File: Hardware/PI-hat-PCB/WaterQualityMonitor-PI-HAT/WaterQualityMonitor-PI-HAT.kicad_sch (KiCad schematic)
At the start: 29 parts

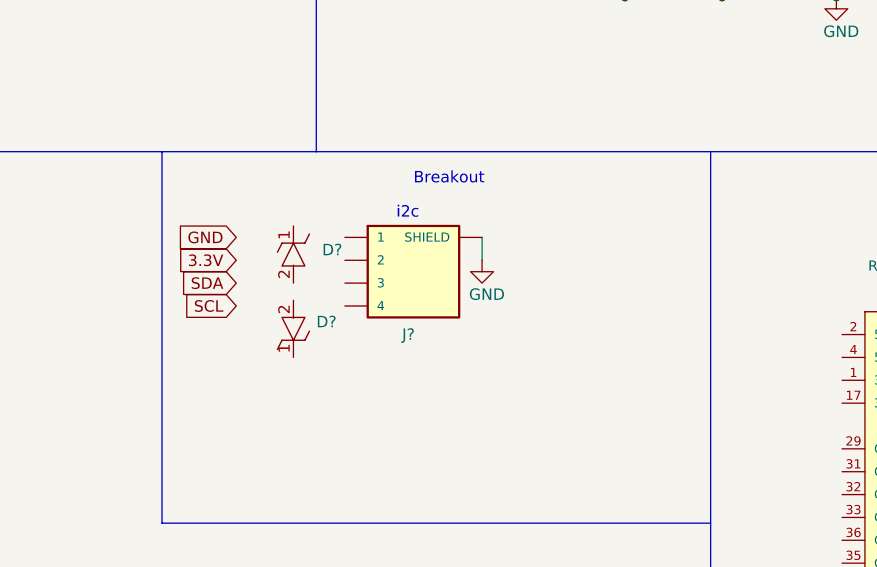
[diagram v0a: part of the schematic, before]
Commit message: updated i2c esd protection circuit
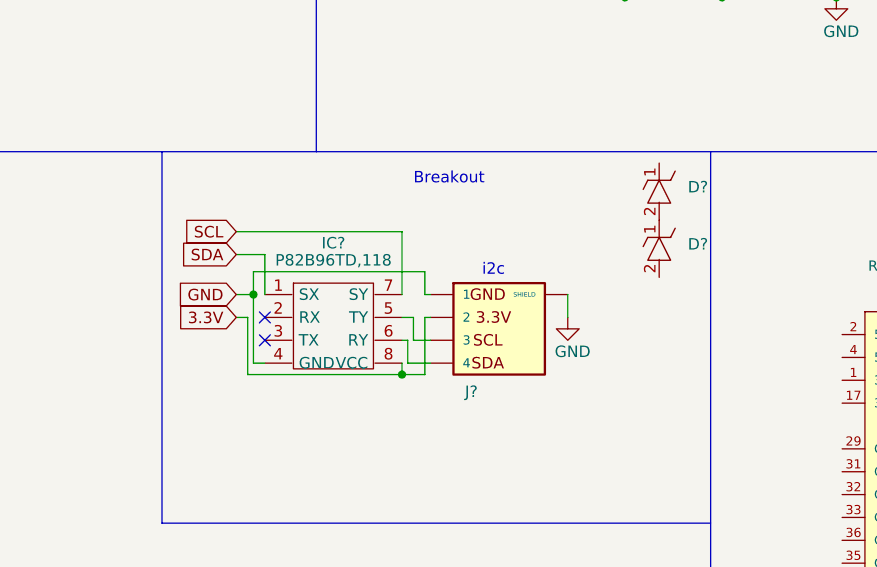
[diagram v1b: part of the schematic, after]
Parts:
- added IC?: P82B96TD,118, SOIC127P600X175-8N, symbol SamacSys_Parts:P82B96TD,118
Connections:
- net 3.3V: now also J?.2, IC?.8 (VCC)
- net GND: now also J?.1, IC?.4 (GND)
- net SCL: now also IC?.7 (SY)
- net SDA: now also IC?.1 (SX)
- net at D?.2: now also D?.1
- net at J?.3: now also IC?.5 (TY)
- net at J?.4: now also IC?.6 (RY)
- no-connect marks 0 -> 2
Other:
- moved on the sheet: D?

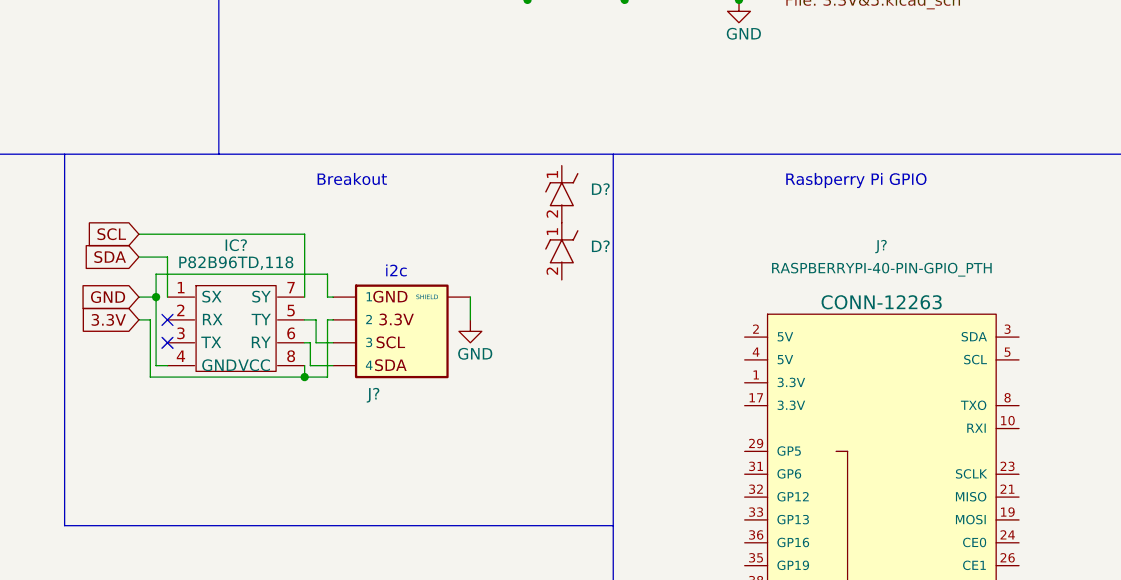
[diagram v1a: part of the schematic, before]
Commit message: fixed i2c circuit
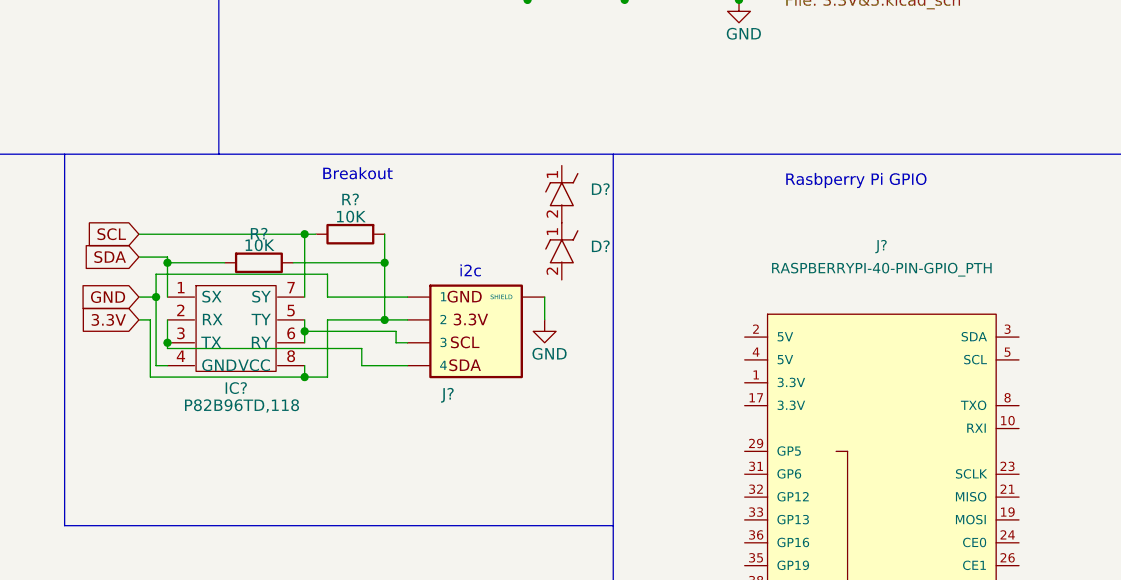
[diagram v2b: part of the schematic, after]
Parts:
- added R? (x2): 10K, symbol Device:R
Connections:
- net 3.3V: now also R?.1, R?.2
- net SCL: now also R?.1
- net SDA: now also R?.2
- net at IC?.2 (RX): now also IC?.3 (TX), J?.4
- net at IC?.5 (TY), J?.3: now also IC?.6 (RY)
- no-connect marks 2 -> 0
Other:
- moved on the sheet: J?

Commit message: log updated
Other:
- note added: "I2C Breakout"
- note removed: "Breakout"
- moved on the sheet: F?
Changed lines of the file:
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@@
     (stroke (width 0) (type default) (color 0 0 0 0))
   )
-  (wire (pts (xy 205.105 32.385) (xy 208.915 32.385))
+  (wire (pts (xy 205.105 32.385) (xy 206.248 32.385))
     (stroke (width 0) (type default) (color 0 0 0 0))
   )
@@
     (stroke (width 0) (type default) (color 0 0 0 0))
   )
+  (wire (pts (xy 213.868 32.385) (xy 216.535 32.385))
+    (stroke (width 0) (type default) (color 0 0 0 0))
+  )
   (wire (pts (xy 63.5 71.755) (xy 67.945 71.755))
     (stroke (width 0) (type default) (color 0 0 0 0))
@@
     (stroke (width 0) (type default) (color 0 0 0 0))
   )
-  (text "Breakout\n" (at 193.675 75.565 0)
+  (text "I2C Breakout\n" (at 187.96 75.565 0)
     (effects (font (size 1.27 1.27)) (justify left bottom))
   )
@@
     (pin "2")
   )
-  (symbol (lib_id "Device:Fuse") (at 212.725 32.385 90) (unit 1)
-    (in_bom yes) (on_board yes) (fields_autoplaced)
-    (property "Reference" "F?" (id 0) (at 212.725 26.035 90))
-    (property "Value" "10A" (id 1) (at 212.725 28.575 90))
-    (property "Footprint" "" (id 2) (at 212.725 34.163 90)
-      (effects (font (size 1.27 1.27)) hide)
-    )
-    (property "Datasheet" "~" (id 3) (at 212.725 32.385 0)
-      (effects (font (size 1.27 1.27)) hide)
-    )
+  (symbol (lib_id "Device:Fuse") (at 210.058 32.385 90) (unit 1)
+    (in_bom yes) (on_board yes) (fields_autoplaced)
+    (property "Reference" "F?" (id 0) (at 210.058 26.035 90))
+    (property "Value" "10A" (id 1) (at 210.058 28.575 90))
+    (property "Footprint" "" (id 2) (at 210.058 34.163 90)
+      (effects (font (size 1.27 1.27)) hide)
+    )
+    (property "Datasheet" "~" (id 3) (at 210.058 32.385 0)
+      (effects (font (size 1.27 1.27)) hide)
+    )

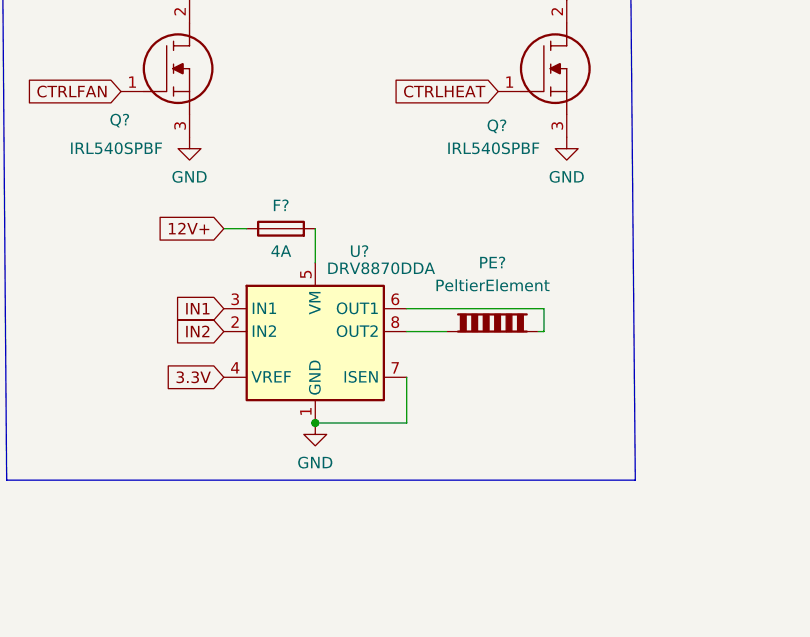
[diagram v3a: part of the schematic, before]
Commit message: Updated H-bridge schematic + Use case diagram
 included decoupling capacitors
Started working on use case diagram
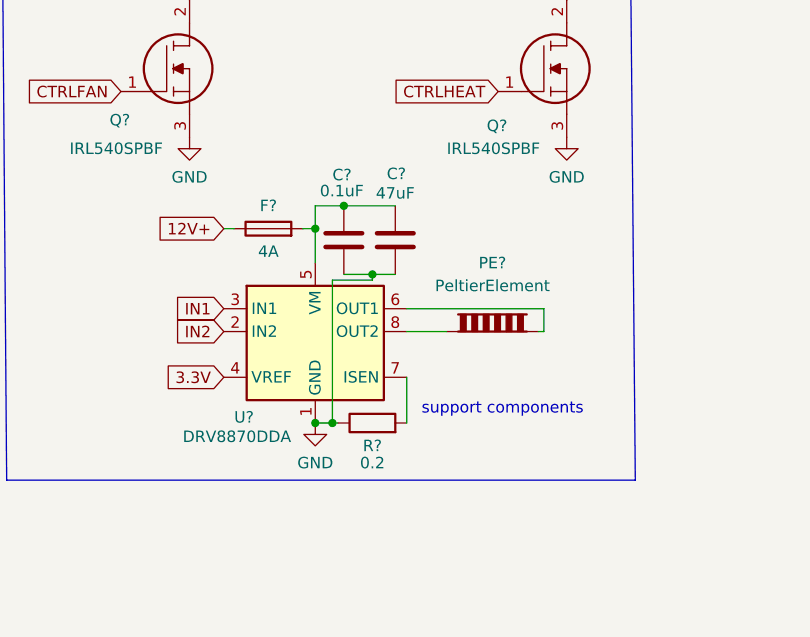
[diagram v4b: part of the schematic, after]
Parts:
- added C?: 47uF, symbol Device:C
- added C?: 0.1uF, symbol Device:C
- added R?: 0.2, symbol Device:R
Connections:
- net GND: now also C?.1, C?.1, R?.1; no longer U?.7 (ISEN)
- net at F?.2, U?.5 (VM): now also C?.2, C?.2
- new net: R?.2, U?.7 (ISEN)
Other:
- note added: "support components"
- moved on the sheet: F?
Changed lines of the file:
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@@
   (junction (at 56.515 27.305) (diameter 0) (color 0 0 0 0)
   )
+  (junction (at 47.625 114.3) (diameter 0) (color 0 0 0 0)
+  )
   (junction (at 30.48 27.305) (diameter 0) (color 0 0 0 0)
   )
@@
   (junction (at 176.53 93.345) (diameter 0) (color 0 0 0 0)
   )
+  (junction (at 53.975 119.38) (diameter 0) (color 0 0 0 0)
+  )
   (junction (at 227.33 55.245) (diameter 0) (color 0 0 0 0)
   )
+  (junction (at 49.53 135.89) (diameter 0) (color 0 0 0 0)
+  )
   (junction (at 175.26 88.265) (diameter 0) (color 0 0 0 0)
   )
+  (junction (at 50.8 111.76) (diameter 0) (color 0 0 0 0)
+  )
   (junction (at 67.818 27.305) (diameter 0) (color 0 0 0 0)
   )
@@
     (stroke (width 0) (type default) (color 0 0 0 0))
   )
+  (wire (pts (xy 53.975 120.015) (xy 49.53 120.015))
+    (stroke (width 0) (type default) (color 0 0 0 0))
+  )
   (polyline (pts (xy 82.55 72.39) (xy 182.245 72.39))
     (stroke (width 0) (type default) (color 0 0 0 0))
@@
     (stroke (width 0) (type default) (color 0 0 0 0))
   )
+  (wire (pts (xy 49.53 135.89) (xy 50.165 135.89))
+    (stroke (width 0) (type default) (color 0 0 0 0))
+  )
   (wire (pts (xy 60.96 45.72) (xy 75.184 45.72))
     (stroke (width 0) (type default) (color 0 0 0 0))
@@
     (stroke (width 0) (type default) (color 0 0 0 0))
   )
-  (wire (pts (xy 37.465 114.3) (xy 40.005 114.3))
+  (wire (pts (xy 47.625 135.89) (xy 49.53 135.89))
+    (stroke (width 0) (type default) (color 0 0 0 0))
+  )
+  (wire (pts (xy 37.465 114.3) (xy 38.608 114.3))
     (stroke (width 0) (type default) (color 0 0 0 0))
   )
@@
     (stroke (width 0) (type default) (color 0 0 0 0))
   )
+  (wire (pts (xy 49.53 120.015) (xy 49.53 135.89))
+    (stroke (width 0) (type default) (color 0 0 0 0))
+  )
   (wire (pts (xy 216.535 55.245) (xy 227.33 55.245))
     (stroke (width 0) (type default) (color 0 0 0 0))
@@
     (stroke (width 0) (type default) (color 0 0 0 0))
   )
+  (wire (pts (xy 53.975 119.38) (xy 56.515 119.38))
+    (stroke (width 0) (type default) (color 0 0 0 0))
+  )
   (wire (pts (xy 174.625 97.155) (xy 191.77 97.155))
     (stroke (width 0) (type default) (color 0 0 0 0))
@@
     (stroke (width 0) (type default) (color 0 0 0 0))
   )
+  (wire (pts (xy 47.625 114.3) (xy 47.625 111.76))
+    (stroke (width 0) (type default) (color 0 0 0 0))
+  )
   (wire (pts (xy 173.355 88.265) (xy 175.26 88.265))
     (stroke (width 0) (type default) (color 0 0 0 0))
@@
     (stroke (width 0) (type default) (color 0 0 0 0))
   )
+  (wire (pts (xy 50.8 111.76) (xy 56.515 111.76))
+    (stroke (width 0) (type default) (color 0 0 0 0))
+  )
   (wire (pts (xy 57.785 130.81) (xy 57.785 135.89))
     (stroke (width 0) (type default) (color 0 0 0 0))
@@
     (stroke (width 0) (type default) (color 0 0 0 0))
   )
+  (wire (pts (xy 53.975 119.38) (xy 53.975 120.015))
+    (stroke (width 0) (type default) (color 0 0 0 0))
+  )
   (wire (pts (xy 175.26 85.725) (xy 194.31 85.725))
     (stroke (width 0) (type default) (color 0 0 0 0))
   )
+  (wire (pts (xy 50.8 119.38) (xy 53.975 119.38))
+    (stroke (width 0) (type default) (color 0 0 0 0))
+  )
   (wire (pts (xy 19.05 27.305) (xy 22.86 27.305))
     (stroke (width 0) (type default) (color 0 0 0 0))
@@
     (stroke (width 0) (type default) (color 0 0 0 0))
   )
-  (wire (pts (xy 57.785 135.89) (xy 47.625 135.89))
-    (stroke (width 0) (type default) (color 0 0 0 0))
-  )
   (wire (pts (xy 56.515 27.305) (xy 56.515 38.1))
     (stroke (width 0) (type default) (color 0 0 0 0))
@@
     (stroke (width 0) (type default) (color 0 0 0 0))
   )
+  (wire (pts (xy 47.625 111.76) (xy 50.8 111.76))
+    (stroke (width 0) (type default) (color 0 0 0 0))
+  )
   (wire (pts (xy 191.77 90.805) (xy 191.77 92.075))
     (stroke (width 0) (type default) (color 0 0 0 0))
   )
   (polyline (pts (xy 226.06 72.39) (xy 226.06 164.465))
+    (stroke (width 0) (type default) (color 0 0 0 0))
+  )
+  (wire (pts (xy 46.228 114.3) (xy 47.625 114.3))
     (stroke (width 0) (type default) (color 0 0 0 0))
   )
@@
   )
   (text "Motors" (at 133.35 16.51 0)
+    (effects (font (size 1.27 1.27)) (justify left bottom))
+  )
+  (text "support components\n" (at 59.436 135.128 0)
     (effects (font (size 1.27 1.27)) (justify left bottom))
   )
@@
       (effects (font (size 1.27 1.27)) (justify right) hide)
     )
+  )
+  (symbol (lib_id "Device:C") (at 56.515 115.57 180) (unit 1)
+    (in_bom yes) (on_board yes)
+    (property "Reference" "C?" (id 0) (at 56.642 108.204 0))
+    (property "Value" "47uF" (id 1) (at 56.515 110.363 0))
+    (property "Footprint" "" (id 2) (at 55.5498 111.76 0)
+      (effects (font (size 1.27 1.27)) hide)
+    )
+    (property "Datasheet" "~" (id 3) (at 56.515 115.57 0)
+      (effects (font (size 1.27 1.27)) hide)
+    )
+    (pin "1")
+    (pin "2")
   )
   (symbol (lib_id "Connector:Screw_Terminal_01x04") (at 179.705 28.575 0) (unit 1)
@@
     (pin "7")
     (pin "8")
+  )
+  (symbol (lib_id "Device:C") (at 50.8 115.57 180) (unit 1)
+    (in_bom yes) (on_board yes)
+    (property "Reference" "C?" (id 0) (at 49.53 108.331 0)
+      (effects (font (size 1.27 1.27)) (justify right))
+    )
+    (property "Value" "0.1uF" (id 1) (at 48.133 110.109 0)
+      (effects (font (size 1.27 1.27)) (justify right))
+    )
+    (property "Footprint" "" (id 2) (at 49.8348 111.76 0)
+      (effects (font (size 1.27 1.27)) hide)
+    )
+    (property "Datasheet" "~" (id 3) (at 50.8 115.57 0)
+      (effects (font (size 1.27 1.27)) hide)
+    )
+    (pin "1")
+    (pin "2")
   )
   (symbol (lib_id "SparkFun-Connectors:RASPBERRYPI-40-PIN-GPIO_PTH") (at 255.905 120.65 0) (unit 1)
@@
     (pin "2")
   )
-  (symbol (lib_id "Device:Fuse") (at 43.815 114.3 90) (unit 1)
-    (in_bom yes) (on_board yes)
-    (property "Reference" "F?" (id 0) (at 43.815 111.76 90))
-    (property "Value" "4A" (id 1) (at 43.815 116.84 90))
-    (property "Footprint" "" (id 2) (at 43.815 116.078 90)
-      (effects (font (size 1.27 1.27)) hide)
-    )
-    (property "Datasheet" "~" (id 3) (at 43.815 114.3 0)
+  (symbol (lib_id "Device:Fuse") (at 42.418 114.3 90) (unit 1)
+    (in_bom yes) (on_board yes)
+    (property "Reference" "F?" (id 0) (at 42.418 111.76 90))
+    (property "Value" "4A" (id 1) (at 42.418 116.84 90))
+    (property "Footprint" "" (id 2) (at 42.418 116.078 90)
+      (effects (font (size 1.27 1.27)) hide)
+    )
+    (property "Datasheet" "~" (id 3) (at 42.418 114.3 0)
       (effects (font (size 1.27 1.27)) hide)
     )
@@
     (pin "2")
   )
+  (symbol (lib_id "Device:R") (at 53.975 135.89 90) (unit 1)
+    (in_bom yes) (on_board yes)
+    (property "Reference" "R?" (id 0) (at 53.975 138.43 90))
+    (property "Value" "0.2" (id 1) (at 53.975 140.335 90))
+    (property "Footprint" "" (id 2) (at 53.975 137.668 90)
+      (effects (font (size 1.27 1.27)) hide)
+    )
+    (property "Datasheet" "~" (id 3) (at 53.975 135.89 0)
+      (effects (font (size 1.27 1.27)) hide)
+    )
+    (pin "1")
+    (pin "2")
+  )
   (symbol (lib_id "Device:Fuse") (at 29.845 72.39 90) (unit 1)
     (in_bom yes) (on_board yes)
@@
   (symbol (lib_id "Driver_Motor:DRV8870DDA") (at 47.625 125.73 0) (unit 1)
     (in_bom yes) (on_board yes)
-    (property "Reference" "U?" (id 0) (at 51.435 116.84 0)
-      (effects (font (size 1.27 1.27)) (justify left))
-    )
-    (property "Value" "DRV8870DDA" (id 1) (at 48.895 118.745 0)
+    (property "Reference" "U?" (id 0) (at 38.608 135.255 0)
+      (effects (font (size 1.27 1.27)) (justify left))
+    )
+    (property "Value" "DRV8870DDA" (id 1) (at 32.893 137.414 0)
       (effects (font (size 1.27 1.27)) (justify left))
     )
@@
       (reference "#PWR?") (unit 1) (value "GND") (footprint "")
     )
+    (path "/023fab8f-e850-4f6d-bd01-c197d7adaf26"
+      (reference "C?") (unit 1) (value "47uF") (footprint "")
+    )
     (path "/2ed95514-5eec-42d9-b793-cef8be4211a9/0f4fd65c-b657-47ac-aaae-e2509ef0f4ff"
       (reference "C?") (unit 1) (value "10u") (footprint "")
@@
       (reference "C?") (unit 1) (value "0.1uF") (footprint "")
     )
+    (path "/6e705e76-606c-4ed6-ae7f-ed966b630818"
+      (reference "C?") (unit 1) (value "0.1uF") (footprint "")
+    )
     (path "/6c4087b1-d585-4615-84b3-d395a8b5856d/7514df18-9295-4870-9b15-d0d13f5e8b8b"
       (reference "C?") (unit 1) (value "100n") (footprint "")
@@
       (reference "R?") (unit 1) (value "178k") (footprint "")
     )
+    (path "/b982913b-78ea-41c6-92bb-058d05052eaf"
+      (reference "R?") (unit 1) (value "0.2") (footprint "")
+    )
     (path "/cb7fd693-d799-4afd-af49-3ab48484f6ca"
